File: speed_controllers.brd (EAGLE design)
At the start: 147.3 x 147.3 mm, 48 parts, among them M1 TE-1-1123723-3, M2 TE-1-1123723-3, M3 TE-1-1123723-3, M4 TE-1-1123723-3, M5 TE-1-1123723-3, M6 TE-1-1123723-3, M7 TE-1-1123723-3, M8 TE-1-1123723-3

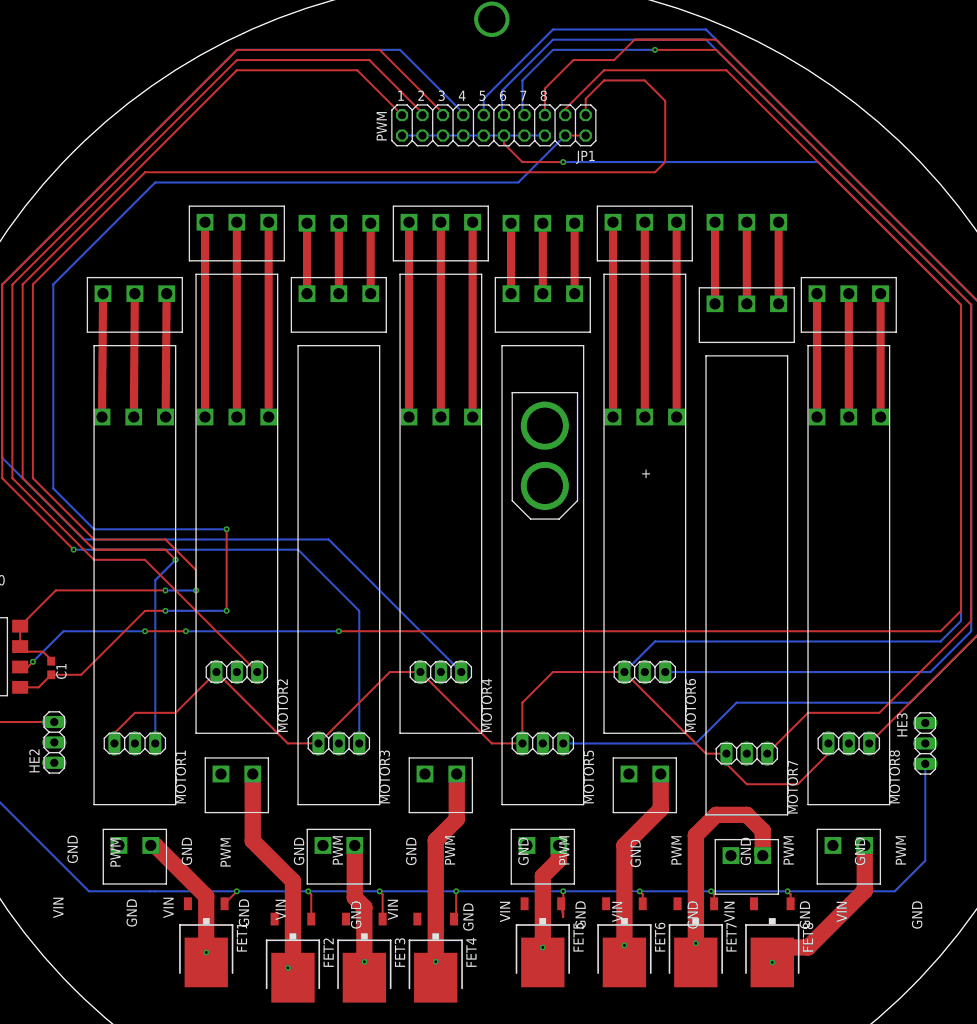
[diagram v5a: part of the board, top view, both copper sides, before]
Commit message: Fix silkscreen
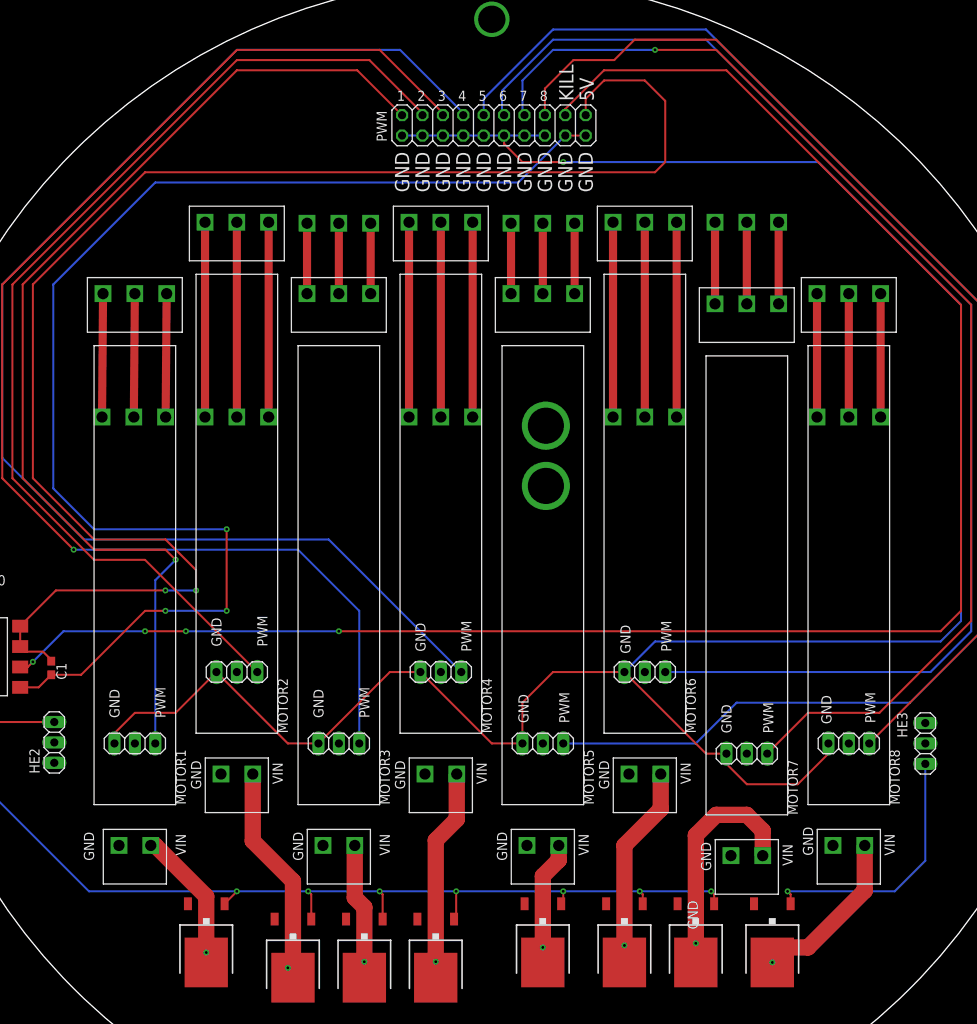
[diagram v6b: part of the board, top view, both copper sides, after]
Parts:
- moved U$1 0.13 mm to (6.73, 14.2), flipped to the bottom
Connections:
- net GND: now also U$1.P$1; no longer U$1.P$2
- net VCC: now also U$1.P$2; no longer U$1.P$1
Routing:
- net FET_G: track 188.0 -> 175.2 mm
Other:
- board text added: "-"
- board text added: "5V"
- board text added: "KILL"

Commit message: Redo routing
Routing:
- net SIG_4: track 162.8 -> 70.3 mm
- net SIG_3: track 162.4 -> 82.7 mm, vias 1 -> 0
- net MCU_VCC: track 189.3 -> 127.3 mm, vias 2 -> 1
- net SIG_2: track 130.2 -> 83.4 mm
- net MCU_GND: track 162.9 -> 118.0 mm, vias 3 -> 1
- net SIG_1: track 131.9 -> 109.6 mm, vias 1 -> 0
- net PWM_GND: track 288.3 -> 281.9 mm
- net KILL_SWITCH_OPTO: vias 4 -> 2
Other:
- board text added: "VCC"
